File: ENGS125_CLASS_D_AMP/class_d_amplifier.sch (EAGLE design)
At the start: 31 parts, among them J1 BANANA_JACK_CT3151, J2 BANANA_JACK_CT3151, J3 BANANA_JACK_CT3151, J4 BANANA_JACK_CT3151, J5 BANANA_JACK_CT3151, J6 BANANA_JACK_CT3151, M1 BSC050NE2LSATMA1, M2 BSC050NE2LSATMA1, U1 LTC6992TSOT-23, U2 LTC4442-MSOP8

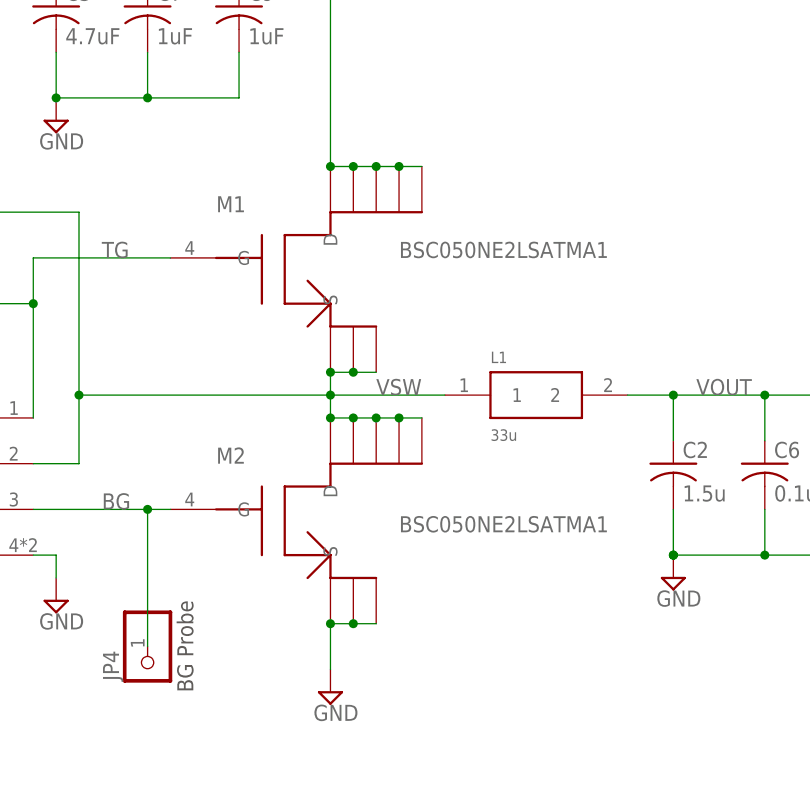
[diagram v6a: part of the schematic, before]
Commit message: Updated MOSFET symbol to use single pins for multiple pads.
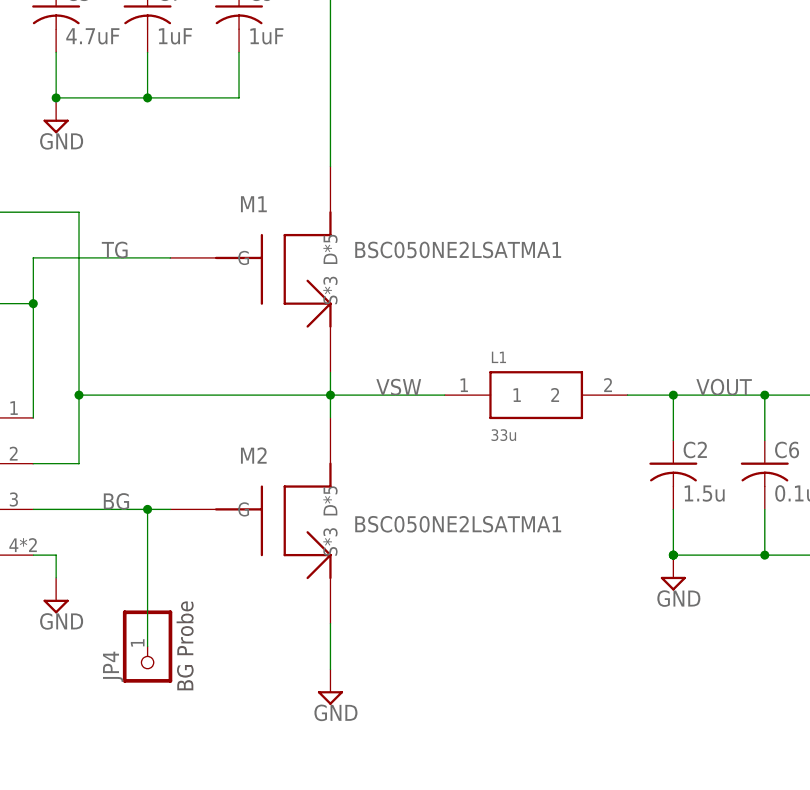
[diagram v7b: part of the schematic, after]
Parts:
- M1, M2: device Engs125_lib_UPDATEFeb22:BSC050NE2LSATMA1 -> Engs125_lib_NEW_UPDATE_USE_THIS_V2:BSC050NE2LSATMA1
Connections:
- net GND: now also M2.S*3; no longer M2.S, M2.S1, M2.S2
- net VIN: now also M1.D*5; no longer M1.D, M1.D1, M1.D2, M1.D3, M1.D4
- net VSW: now also M1.S*3, M2.D*5; no longer M1.S, M1.S1, M1.S2, M2.D, M2.D1, M2.D2, M2.D3, M2.D4
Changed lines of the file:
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@@
 <setting verticaltext="up"/>
 </settings>
-<grid distance="0.1" unitdist="inch" unit="inch" style="lines" multiple="1" display="no" altdistance="0.01" altunitdist="inch" altunit="inch"/>
+<grid distance="0.1" unitdist="inch" unit="inch" style="lines" multiple="1" display="yes" altdistance="0.01" altunitdist="inch" altunit="inch"/>
 <layers>
 <layer number="1" name="Top" color="4" fill="1" visible="no" active="no"/>
@@
 <part name="R2" library="Engs125_lib_UPDATEFeb22" deviceset="R-US" device="" value=""/>
 <part name="JP2" library="Engs125_lib_UPDATEFeb22" deviceset="PINHD-1X1" device=""/>
-<part name="M1" library="Engs125_lib_UPDATEFeb22" deviceset="BSC050NE2LSATMA1" device=""/>
-<part name="M2" library="Engs125_lib_UPDATEFeb22" deviceset="BSC050NE2LSATMA1" device=""/>
 <part name="J5" library="Engs125_lib_UPDATEFeb22" deviceset="BANANA_JACK_CT3151" device=""/>
 <part name="J6" library="Engs125_lib_UPDATEFeb22" deviceset="BANANA_JACK_CT3151" device=""/>
@@
 <part name="SUPPLY2" library="Engs125_library" deviceset="GND" device=""/>
 <part name="U2" library="Engs125_lib_NEW_UPDATE_USE_THIS_V2" deviceset="LTC4442" device="" value="LTC4442-MSOP8"/>
+<part name="M1" library="Engs125_lib_NEW_UPDATE_USE_THIS_V2" deviceset="BSC050NE2LSATMA1" device=""/>
+<part name="M2" library="Engs125_lib_NEW_UPDATE_USE_THIS_V2" deviceset="BSC050NE2LSATMA1" device=""/>
 </parts>
 <sheets>
@@
 <attribute name="VALUE" x="57.15" y="43.18" size="1.778" layer="96"/>
 </instance>
-<instance part="M1" gate="G$1" x="124.46" y="93.98" smashed="yes">
-<attribute name="NAME" x="116.84" y="99.06" size="1.778" layer="96"/>
-<attribute name="VALUE" x="137.16" y="93.98" size="1.778" layer="96"/>
-</instance>
-<instance part="M2" gate="G$1" x="124.46" y="66.04" smashed="yes">
-<attribute name="NAME" x="116.84" y="71.12" size="1.778" layer="96"/>
-<attribute name="VALUE" x="137.16" y="63.5" size="1.778" layer="96"/>
-</instance>
 <instance part="J5" gate="G$1" x="213.36" y="78.74" smashed="yes" rot="R180">
 <attribute name="VALUE" x="214.06" y="82.24" size="0.8128" layer="96" rot="R180"/>
@@
 <attribute name="NAME" x="73.66" y="79.248" size="1.778" layer="95"/>
 <attribute name="VALUE" x="73.66" y="55.88" size="1.778" layer="96"/>
+</instance>
+<instance part="M1" gate="G$1" x="121.92" y="93.98" smashed="yes">
+<attribute name="NAME" x="119.38" y="99.06" size="1.778" layer="95"/>
+<attribute name="VALUE" x="132.08" y="93.98" size="1.778" layer="96"/>
+</instance>
+<instance part="M2" gate="G$1" x="121.92" y="66.04" smashed="yes">
+<attribute name="NAME" x="119.38" y="71.12" size="1.778" layer="95"/>
+<attribute name="VALUE" x="132.08" y="63.5" size="1.778" layer="96"/>
 </instance>
 </instances>
@@
 <segment>
 <pinref part="SUPPLY9" gate="GND" pin="GND"/>
-<pinref part="M2" gate="G$1" pin="S"/>
-<junction x="129.54" y="53.34"/>
-<pinref part="M2" gate="G$1" pin="S2"/>
-<wire x1="134.62" y1="53.34" x2="132.08" y2="53.34" width="0.1524" layer="91"/>
-<pinref part="M2" gate="G$1" pin="S1"/>
-<junction x="132.08" y="53.34"/>
-<wire x1="132.08" y1="53.34" x2="129.54" y2="53.34" width="0.1524" layer="91"/>
 <wire x1="129.54" y1="53.34" x2="129.54" y2="48.26" width="0.1524" layer="91"/>
+<pinref part="M2" gate="G$1" pin="S*3"/>
 </segment>
 <segment>
@@
 <junction x="101.6" y="78.74"/>
 <label x="134.62" y="78.74" size="1.778" layer="95"/>
-<pinref part="M1" gate="G$1" pin="S"/>
-<pinref part="M2" gate="G$1" pin="D"/>
-<pinref part="M2" gate="G$1" pin="D2"/>
-<wire x1="134.62" y1="76.2" x2="132.08" y2="76.2" width="0.1524" layer="91"/>
-<junction x="129.54" y="76.2"/>
-<pinref part="M2" gate="G$1" pin="D1"/>
-<wire x1="132.08" y1="76.2" x2="129.54" y2="76.2" width="0.1524" layer="91"/>
-<junction x="132.08" y="76.2"/>
-<pinref part="M1" gate="G$1" pin="S2"/>
-<wire x1="134.62" y1="81.28" x2="132.08" y2="81.28" width="0.1524" layer="91"/>
-<junction x="129.54" y="81.28"/>
-<pinref part="M1" gate="G$1" pin="S1"/>
-<wire x1="132.08" y1="81.28" x2="129.54" y2="81.28" width="0.1524" layer="91"/>
-<junction x="132.08" y="81.28"/>
-<pinref part="M2" gate="G$1" pin="D4"/>
-<wire x1="134.62" y1="76.2" x2="137.16" y2="76.2" width="0.1524" layer="91"/>
-<junction x="134.62" y="76.2"/>
-<pinref part="M2" gate="G$1" pin="D3"/>
-<wire x1="137.16" y1="76.2" x2="139.7" y2="76.2" width="0.1524" layer="91"/>
-<junction x="137.16" y="76.2"/>
 <pinref part="U2" gate="G$1" pin="TS"/>
+<pinref part="M1" gate="G$1" pin="S*3"/>
+<pinref part="M2" gate="G$1" pin="D*5"/>
 </segment>
 </net>
@@
 <wire x1="99.06" y1="129.54" x2="99.06" y2="124.46" width="0.1524" layer="91"/>
 <pinref part="J3" gate="G$1" pin="IN"/>
-<pinref part="M1" gate="G$1" pin="D"/>
-<pinref part="M1" gate="G$1" pin="D2"/>
-<wire x1="134.62" y1="104.14" x2="132.08" y2="104.14" width="0.1524" layer="91"/>
-<junction x="129.54" y="104.14"/>
-<pinref part="M1" gate="G$1" pin="D1"/>
-<wire x1="132.08" y1="104.14" x2="129.54" y2="104.14" width="0.1524" layer="91"/>
-<junction x="132.08" y="104.14"/>
-<pinref part="M1" gate="G$1" pin="D4"/>
-<wire x1="134.62" y1="104.14" x2="137.16" y2="104.14" width="0.1524" layer="91"/>
-<junction x="134.62" y="104.14"/>
-<pinref part="M1" gate="G$1" pin="D3"/>
-<wire x1="137.16" y1="104.14" x2="139.7" y2="104.14" width="0.1524" layer="91"/>
-<junction x="137.16" y="104.14"/>
 <pinref part="C9" gate="G$1" pin="1"/>
 <wire x1="119.38" y1="124.46" x2="119.38" y2="129.54" width="0.1524" layer="91"/>
 <junction x="119.38" y="129.54"/>
+<pinref part="M1" gate="G$1" pin="D*5"/>
 </segment>
 </net>
@@
 <segment>
 <label x="104.14" y="66.04" size="1.778" layer="95"/>
-<pinref part="M2" gate="G$1" pin="G"/>
 <wire x1="96.52" y1="66.04" x2="109.22" y2="66.04" width="0.1524" layer="91"/>
 <pinref part="JP4" gate="G$1" pin="1"/>
@@
 <junction x="109.22" y="66.04"/>
 <pinref part="U2" gate="G$1" pin="BG"/>
+<pinref part="M2" gate="G$1" pin="G"/>
 </segment>
 </net>
@@
 <wire x1="96.52" y1="93.98" x2="111.76" y2="93.98" width="0.1524" layer="91"/>
 <label x="104.14" y="93.98" size="1.778" layer="95"/>
-<pinref part="M1" gate="G$1" pin="G"/>
 <pinref part="JP3" gate="G$1" pin="1"/>
 <wire x1="81.28" y1="88.9" x2="96.52" y2="88.9" width="0.1524" layer="91"/>
 <junction x="96.52" y="88.9"/>
 <pinref part="U2" gate="G$1" pin="TG"/>
-</segment>
-</net>
+<pinref part="M1" gate="G$1" pin="G"/>
+</segment>
+</net>
